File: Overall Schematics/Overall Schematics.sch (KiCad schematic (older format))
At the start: 1 part, among them U1 Teensy4.1

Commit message: added motor schematics
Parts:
- added M? (x2): Stepper_Motor_bipolar, symbol Motor:Stepper_Motor_bipolar
- added M? (x4): Motor_DC, symbol Motor:Motor_DC
- added U? (x4): VNH52019, symbol CustomLibrary:VNH52019
- added U? (x2): StepperMotorDriver, symbol CustomLibrary:StepperMotorDriver
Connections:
- net labels added: +3V3, +5V, +6V, +8V, GND
- wire segments 0 -> 196
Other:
- moved on the sheet: U1

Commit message: edited some voltage and name of stepper motor
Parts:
- U? (x2): value StepperMotorDriver -> 36v4SMD
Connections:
- net labels added: +24V
- net labels removed: +5V, +6V, +8V
- wire segments 196 -> 198
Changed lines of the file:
@@
-	1    0    0    -1
-$EndComp
-$Comp
-L CustomLibrary:StepperMotorDriver U?
-U 1 1 5F98ED02
-P 5900 550
-F 0 "U?" H 5900 613 50  0000 C CNN
-F 1 "StepperMotorDriver" H 5900 522 50  0000 C CNN
-F 2 "" H 5900 550 50  0001 C CNN
-F 3 "" H 5900 550 50  0001 C CNN
-	1    5900 550
 	1    0    0    -1
 $EndComp
@@
 P 5950 1650
 F 0 "U?" H 5950 1713 50  0000 C CNN
-F 1 "StepperMotorDriver" H 5950 1622 50  0000 C CNN
+F 1 "36v4SMD" H 5950 1622 50  0000 C CNN
 F 2 "" H 5950 1650 50  0001 C CNN
 F 3 "" H 5950 1650 50  0001 C CNN
@@
 	7050 2200 7150 2200
 Wire Wire Line
-	6400 1050 6650 1050
-Wire Wire Line
 	6650 1050 6650 600
 Wire Wire Line
@@
 	7350 600  7350 750
 Wire Wire Line
-	6400 1100 6750 1100
-Wire Wire Line
 	6750 1100 6750 650
 Wire Wire Line
@@
 	7550 650  7550 750
 Wire Wire Line
-	6400 1150 6800 1150
-Wire Wire Line
 	6800 1150 6800 950
 Wire Wire Line
 	6800 950  7150 950
 Wire Wire Line
-	6400 1200 7050 1200
-Wire Wire Line
 	7050 1200 7050 1150
 Wire Wire Line
 	7050 1150 7150 1150
-$Comp
-L power:+8V #PWR?
-U 1 1 5F9BBF7D
-P 6450 800
-F 0 "#PWR?" H 6450 650 50  0001 C CNN
-F 1 "+8V" H 6465 973 50  0000 C CNN
-F 2 "" H 6450 800 50  0001 C CNN
-F 3 "" H 6450 800 50  0001 C CNN
-	1    6450 800
-	1    0    0    -1
-$EndComp
 Wire Wire Line
 	6400 900  6450 900
@@
 Wire Wire Line
 	6450 850  6450 800
-$Comp
-L power:+8V #PWR?
-U 1 1 5F9C2D1E
-P 6500 1850
-F 0 "#PWR?" H 6500 1700 50  0001 C CNN
-F 1 "+8V" H 6515 2023 50  0000 C CNN
-F 2 "" H 6500 1850 50  0001 C CNN
-F 3 "" H 6500 1850 50  0001 C CNN
-	1    6500 1850
-	1    0    0    -1
-$EndComp
 Wire Wire Line
 	6450 2000 6500 2000
@@
 Wire Wire Line
 	6450 3250 6600 3250
-$Comp
-L power:+6V #PWR?
-U 1 1 5F9D338A
-P 6600 3250
-F 0 "#PWR?" H 6600 3100 50  0001 C CNN
-F 1 "+6V" V 6615 3378 50  0000 L CNN
-F 2 "" H 6600 3250 50  0001 C CNN
-F 3 "" H 6600 3250 50  0001 C CNN
-	1    6600 3250
-	0    1    1    0
-$EndComp
-$Comp
-L power:+6V #PWR?
-U 1 1 5F9D863A
-P 6600 3950
-F 0 "#PWR?" H 6600 3800 50  0001 C CNN
-F 1 "+6V" V 6615 4078 50  0000 L CNN
-F 2 "" H 6600 3950 50  0001 C CNN
-F 3 "" H 6600 3950 50  0001 C CNN
-	1    6600 3950
-	0    1    1    0
-$EndComp
-$Comp
-L power:+6V #PWR?
-U 1 1 5F9DB48D
-P 6600 4750
-F 0 "#PWR?" H 6600 4600 50  0001 C CNN
-F 1 "+6V" V 6615 4878 50  0000 L CNN
-F 2 "" H 6600 4750 50  0001 C CNN
-F 3 "" H 6600 4750 50  0001 C CNN
-	1    6600 4750
-	0    1    1    0
-$EndComp
-$Comp
-L power:+6V #PWR?
-U 1 1 5F9DE57B
-P 6600 5600
-F 0 "#PWR?" H 6600 5450 50  0001 C CNN
-F 1 "+6V" V 6615 5728 50  0000 L CNN
-F 2 "" H 6600 5600 50  0001 C CNN
-F 3 "" H 6600 5600 50  0001 C CNN
-	1    6600 5600
-	0    1    1    0
-$EndComp
 Wire Wire Line
 	6450 3950 6600 3950
@@
 	6500 2050 6550 2050
 Wire Wire Line
-	6400 950  6500 950
-Wire Wire Line
-	6400 1000 6500 1000
-Wire Wire Line
 	6500 1000 6500 950
 Connection ~ 6500 950
@@
 Wire Wire Line
 	3450 1150 3550 1150
-$Comp
-L power:+5V #PWR?
-U 1 1 5FACD3DC
-P 3550 1000
-F 0 "#PWR?" H 3550 850 50  0001 C CNN
-F 1 "+5V" H 3565 1173 50  0000 C CNN
-F 2 "" H 3550 1000 50  0001 C CNN
-F 3 "" H 3550 1000 50  0001 C CNN
-	1    3550 1000
-	1    0    0    -1
-$EndComp
 Wire Wire Line
 	3450 1050 3550 1050
@@
 Wire Wire Line
 	900  3050 1250 3050
+$Comp
+L power:+24V #PWR?
+U 1 1 5F9D807E
+P 3500 850
+F 0 "#PWR?" H 3500 700 50  0001 C CNN
+F 1 "+24V" H 3515 1023 50  0000 C CNN
+F 2 "" H 3500 850 50  0001 C CNN
+F 3 "" H 3500 850 50  0001 C CNN
+	1    3500 850
+	1    0    0    -1
+$EndComp
+Wire Wire Line
+	3450 900  3500 900
+Wire Wire Line
+	3500 900  3500 850
+Wire Wire Line
+	6400 1200 7050 1200
+Wire Wire Line
+	6400 1150 6800 1150
+Wire Wire Line
+	6400 1100 6750 1100
+Wire Wire Line
+	6400 1050 6650 1050
+Wire Wire Line
+	6400 1000 6500 1000
+Wire Wire Line
+	6400 950  6500 950
+$Comp
+L CustomLibrary:StepperMotorDriver U?
+U 1 1 5F98ED02
+P 5900 550
+F 0 "U?" H 5900 613 50  0000 C CNN
+F 1 "36v4SMD" H 5900 522 50  0000 C CNN
+F 2 "" H 5900 550 50  0001 C CNN
+F 3 "" H 5900 550 50  0001 C CNN
+	1    5900 550
+	1    0    0    -1
+$EndComp
+$Comp
+L power:+24V #PWR?
+U 1 1 5FA0453E
+P 6450 800
+F 0 "#PWR?" H 6450 650 50  0001 C CNN
+F 1 "+24V" H 6465 973 50  0000 C CNN
+F 2 "" H 6450 800 50  0001 C CNN
+F 3 "" H 6450 800 50  0001 C CNN
+	1    6450 800
+	1    0    0    -1
+$EndComp
+$Comp
+L power:+24V #PWR?
+U 1 1 5FA11C95
+P 6500 1850
+F 0 "#PWR?" H 6500 1700 50  0001 C CNN
+F 1 "+24V" H 6515 2023 50  0000 C CNN
+F 2 "" H 6500 1850 50  0001 C CNN
+F 3 "" H 6500 1850 50  0001 C CNN
+	1    6500 1850
+	1    0    0    -1
+$EndComp
+$Comp
+L power:+24V #PWR?
+U 1 1 5FA1F45E
+P 6600 3250
+F 0 "#PWR?" H 6600 3100 50  0001 C CNN
+F 1 "+24V" V 6615 3378 50  0000 L CNN
+F 2 "" H 6600 3250 50  0001 C CNN
+F 3 "" H 6600 3250 50  0001 C CNN
+	1    6600 3250
+	0    1    1    0
+$EndComp
+$Comp
+L power:+24V #PWR?
+U 1 1 5FA54773
+P 6600 4750
+F 0 "#PWR?" H 6600 4600 50  0001 C CNN
+F 1 "+24V" V 6615 4878 50  0000 L CNN
+F 2 "" H 6600 4750 50  0001 C CNN
+F 3 "" H 6600 4750 50  0001 C CNN
+	1    6600 4750
+	0    1    1    0
+$EndComp
+$Comp
+L power:+24V #PWR?
+U 1 1 5FA6150A
+P 6600 3950
+F 0 "#PWR?" H 6600 3800 50  0001 C CNN
+F 1 "+24V" V 6615 4078 50  0000 L CNN
+F 2 "" H 6600 3950 50  0001 C CNN
+F 3 "" H 6600 3950 50  0001 C CNN
+	1    6600 3950
+	0    1    1    0
+$EndComp
+$Comp
+L power:+24V #PWR?
+U 1 1 5FA7B478
+P 6600 5600
+F 0 "#PWR?" H 6600 5450 50  0001 C CNN
+F 1 "+24V" V 6615 5728 50  0000 L CNN
+F 2 "" H 6600 5600 50  0001 C CNN
+F 3 "" H 6600 5600 50  0001 C CNN
+	1    6600 5600
+	0    1    1    0
+$EndComp
 $EndSCHEMATC

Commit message: made some changes
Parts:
- U? (x2): symbol CustomLibrary:StepperMotorDriver -> Overall-Schematics-rescue:StepperMotorDriver-CustomLibrary
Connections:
- net labels added: +3.3V, DIR_1, PWR_GND, STEP_1
- wire segments 198 -> 146
- no-connect marks 0 -> 28

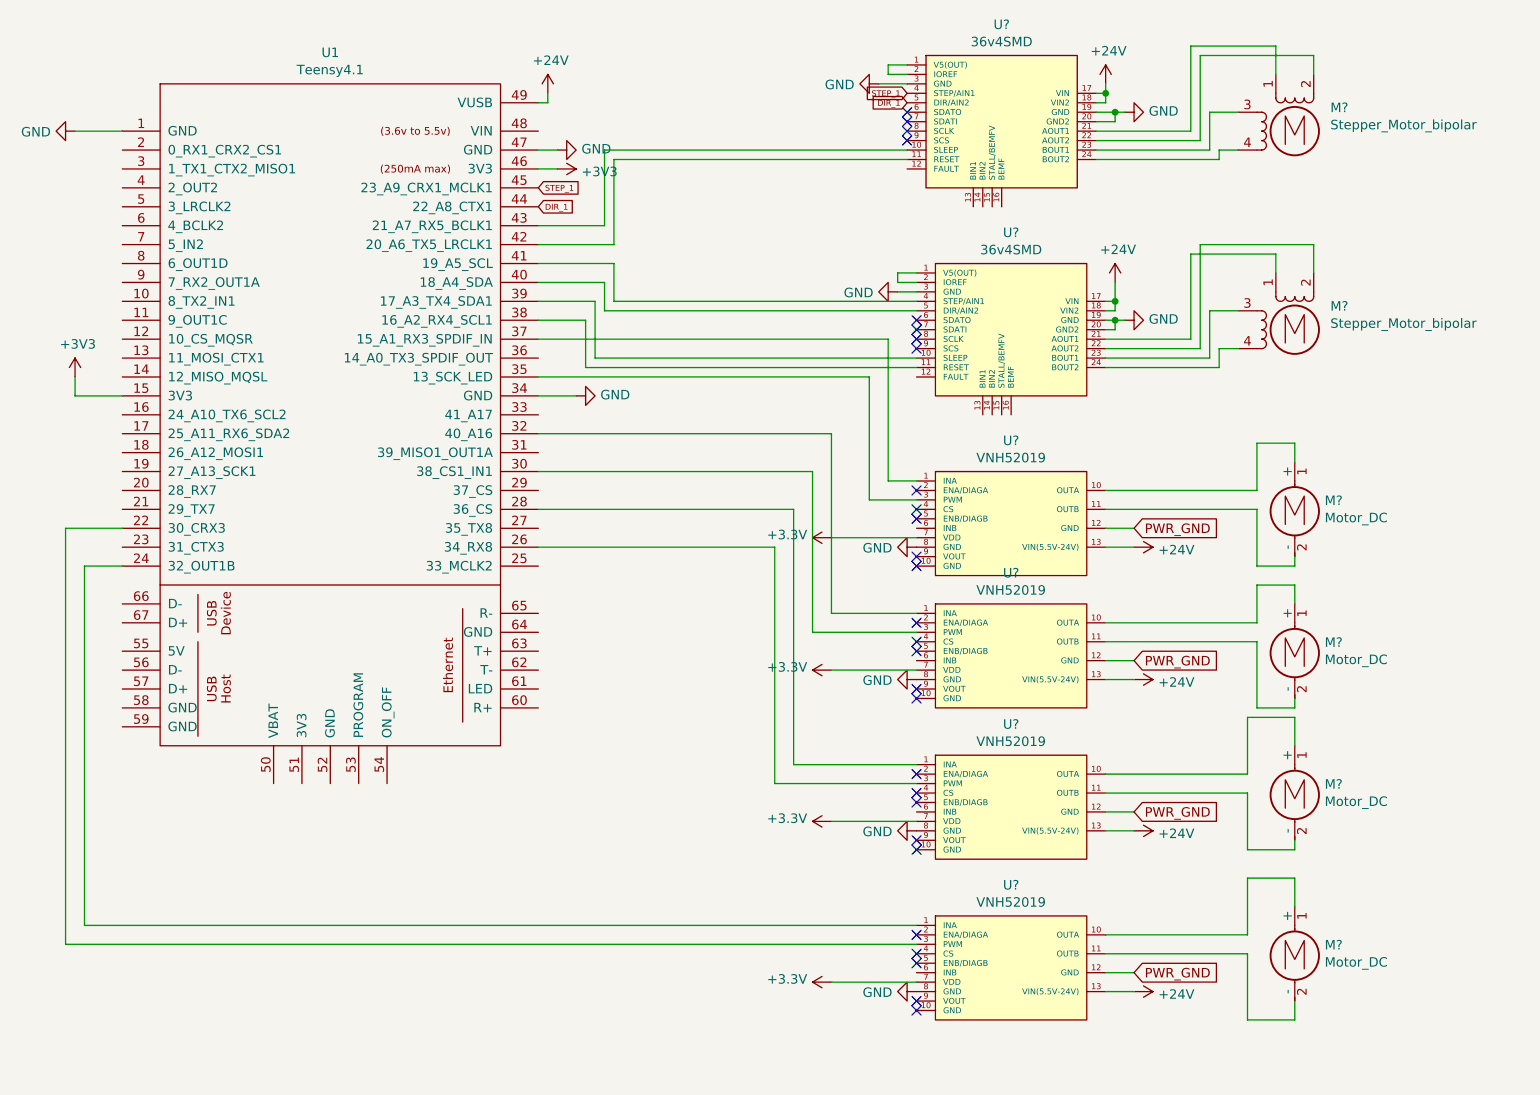
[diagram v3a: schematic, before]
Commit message: adding labels to pins
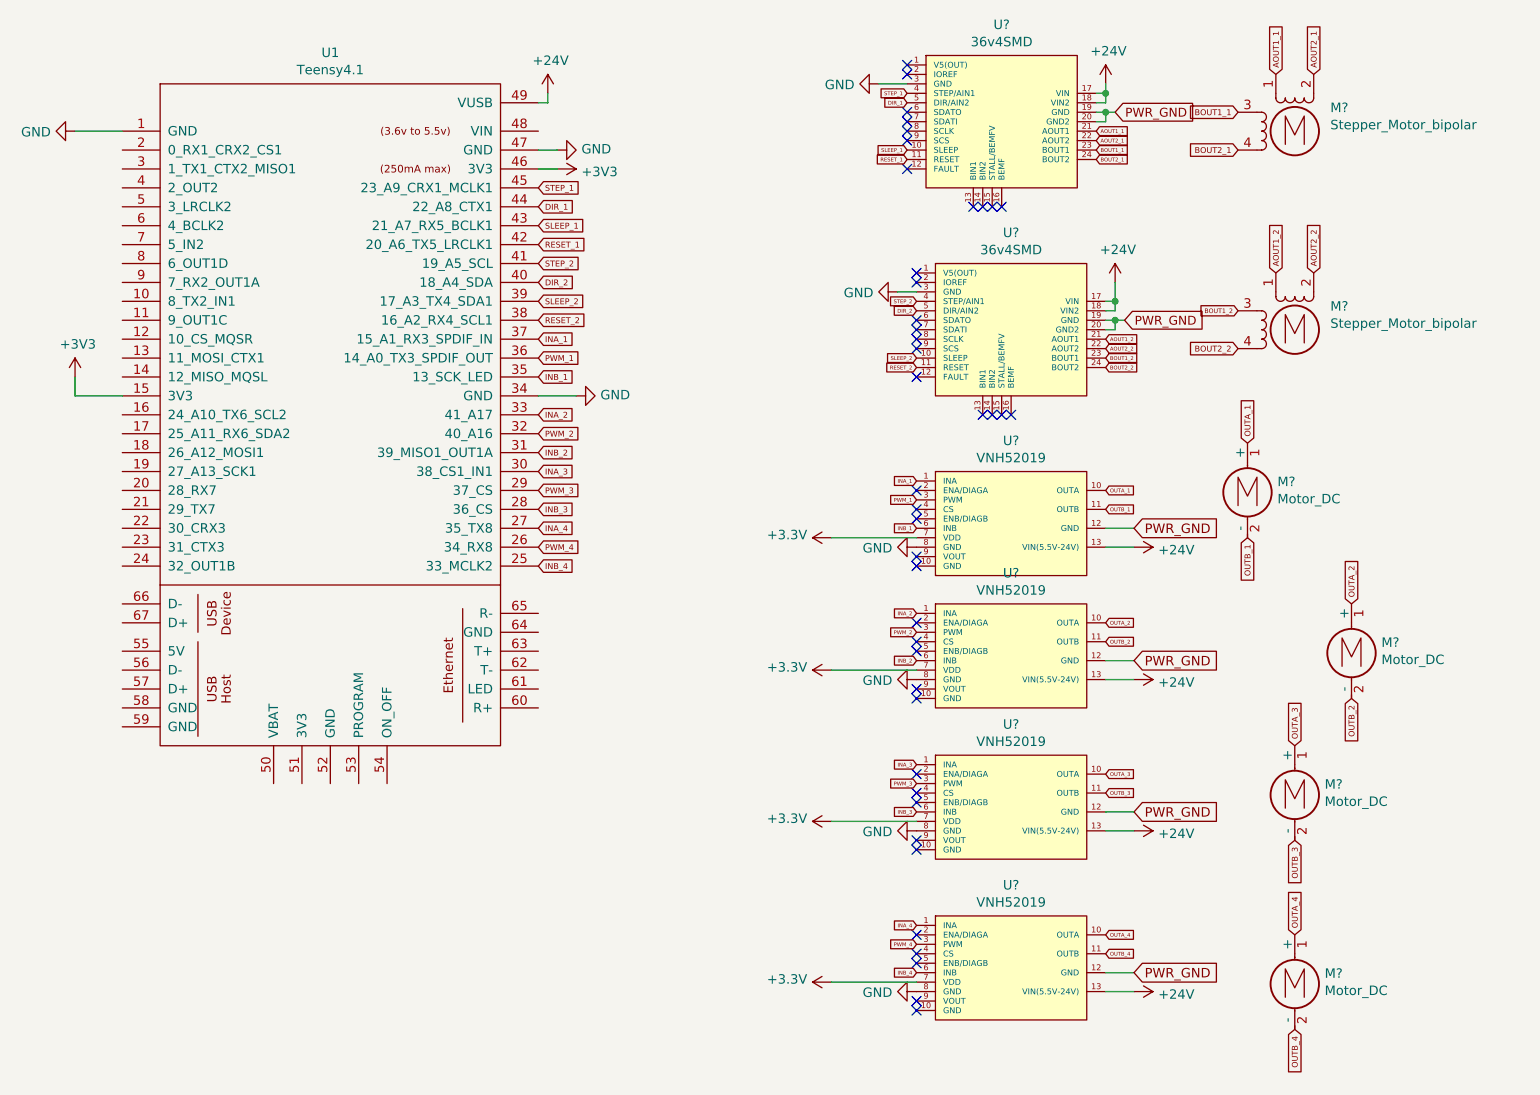
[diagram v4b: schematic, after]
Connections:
- net GND: no longer U?.19 (GND), U?.19 (GND), U?.20 (GND2), U?.20 (GND2)
- net PWR_GND: now also U?.19 (GND), U?.19 (GND), U?.20 (GND2), U?.20 (GND2)
- net at U1.22 (30_CRX3): no longer U?.3 (PWM)
- net at U1.24 (32_OUT1B): no longer U?.1 (INA)
- net INB_4: now reaches U1.25 (33_MCLK2)
- net INB_4: now also U?.6 (INB)
- net PWM_3: now reaches U?.3 (PWM)
- net PWM_3: now also U1.29 (37_CS); no longer U1.26 (34_RX8)
- net INA_4: now reaches U1.27 (35_TX8)
- net INA_4: now also U?.1 (INA)
- net INA_3: now reaches U?.1 (INA)
- net INA_3: now also U1.30 (38_CS1_IN1); no longer U1.28 (36_CS)
- net PWM_2: now reaches U?.3 (PWM)
- net PWM_2: now also U1.32 (40_A16); no longer U1.30 (38_CS1_IN1)
- net INB_2: now reaches U1.31 (39_MISO1_OUT1A)
- net INB_2: now also U?.6 (INB)
- net INA_2: now reaches U?.1 (INA)
- net INA_2: now also U1.33 (41_A17); no longer U1.32 (40_A16)
- net INB_1: now reaches U1.35 (13_SCK_LED)
- net INB_1: now also U?.6 (INB); no longer U?.3 (PWM)
- net PWM_1: now reaches U1.36 (14_A0_TX3_SPDIF_OUT)
- net PWM_1: now also U?.3 (PWM)
- net INA_1: now reaches U1.37 (15_A1_RX3_SPDIF_IN), U?.1 (INA)
- net RESET_2: now reaches U1.38 (16_A2_RX4_SCL1), U?.11 (RESET)
- net SLEEP_2: now reaches U1.39 (17_A3_TX4_SDA1), U?.10 (SLEEP)
- net DIR_2: now reaches U1.40 (18_A4_SDA), U?.5 (DIR/AIN2)
- net STEP_2: now reaches U1.41 (19_A5_SCL), U?.4 (STEP/AIN1)
- net RESET_1: now reaches U1.42 (20_A6_TX5_LRCLK1), U?.11 (RESET)
- net SLEEP_1: now reaches U1.43 (21_A7_RX5_BCLK1), U?.10 (SLEEP)
- net OUTA_1: now reaches U?.10 (OUTA)
- net OUTA_1: now also M?.1 (+)
- net OUTB_1: now reaches M?.2 (-), U?.11 (OUTB)
- net OUTA_2: now reaches U?.10 (OUTA)
- net OUTA_2: now also M?.1 (+)
- net OUTB_2: now reaches M?.2 (-), U?.11 (OUTB)
- net OUTA_3: now reaches U?.10 (OUTA)
- net OUTA_3: now also M?.1 (+)
- net OUTB_3: now reaches M?.2 (-), U?.11 (OUTB)
- net INB_3: now reaches U?.6 (INB)
- net INB_3: now also U1.28 (36_CS)
- net OUTA_4: now reaches U?.10 (OUTA)
- net OUTA_4: now also M?.1 (+)
- net OUTB_4: now reaches M?.2 (-), U?.11 (OUTB)
- net at U?.1 (V5(OUT)): no longer U?.2 (IOREF) (x2)
- net AOUT1_1: now reaches M?.1, U?.21 (AOUT1)
- net AOUT2_1: now reaches M?.2 (-), U?.22 (AOUT2)
- net BOUT1_1: now reaches M?.3, U?.23 (BOUT1)
- net BOUT2_1: now reaches M?.4, U?.24 (BOUT2)
- net AOUT1_2: now reaches M?.1, U?.21 (AOUT1)
- net AOUT2_2: now reaches M?.2 (-), U?.22 (AOUT2)
- net BOUT1_2: now reaches M?.3, U?.23 (BOUT1)
- net BOUT2_2: now reaches M?.4, U?.24 (BOUT2)
- new net PWM_4: U1.26 (34_RX8), U?.3 (PWM)
- no-connect marks 28 -> 42
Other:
- moved on the sheet: M?

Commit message: made area bigger
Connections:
- net OUTA_1: no longer M?.1 (+)
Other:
- note added: "Stepper Motors"
- moved on the sheet: M?, U1, U?
